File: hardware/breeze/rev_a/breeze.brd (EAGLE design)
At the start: 27.2 x 14.2 mm, 11 parts, among them J3 IMPULSE_GECKO_HEADER, U1 RV-3049-C3, U2 FM25V20-DG

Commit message: some parts on breeze
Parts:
- removed BT1: ML-1220/F1AN, batteries:ML-1220/F1BN
- removed C1: 10nF, passives:0402_CAP
- removed C2: 0.1uF, passives:0402_CAP
- removed R1, R2: 4.7k, passives:0402_RES
- removed R3, R4: 10k, passives:0402_RES
- removed U1: RV-3049-C3, chips:MICRO-CRYSTAL-C3
- removed U2: FM25V20-DG, chips:TDFN-8/6MM
- added Q1: NX3008PBK, fets:SOT23-3
- added R6: 100k, rcl:R0603
- moved LOGO1 5.76 mm to (2.69, 15.9)
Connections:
- removed net !FRAM_CS: J3.2, R1.1, U2.1
- removed net BATTERY: BT1.POS, C1.1, U1.2
- removed net N$6: R4.2, U1.9
- removed net N$7: R3.2, U1.1
- removed net RTC_CS: J3.4, R2.2, U1.8
- new net AIRFLOW_CTRL: J3.4, Q1.1, R6.1
- new net AIRFLOW_VCC: Q1.2
- new net TRIGGER: J3.2
- net GND: no longer BT1.NEG, C1.2, C2.2, R2.1, R3.1, R4.1, U1.6, U2.4
- net MISO0: no longer U1.5, U2.2
- net MOSI0: no longer U1.10, U2.5
- net SCLK0: no longer U1.4, U2.6
- net VCC: now also Q1.3, R6.2; no longer C2.1, R1.2, U2.3, U2.7, U2.8
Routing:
- net VCC: track 26.3 -> 0.00 mm, vias 3 -> 0
- net MISO0: track 23.9 -> 0.00 mm, vias 2 -> 0
- net !FRAM_CS: track 20.9 -> 0.00 mm, vias 2 -> 0
- net MOSI0: track 17.4 -> 0.00 mm, vias 2 -> 0
- net SCLK0: track 15.0 -> 0.00 mm
- net RTC_CS: track 6.19 -> 0.00 mm
- net BATTERY: track 5.69 -> 0.00 mm
- net GND: track 2.38 -> 0.00 mm, vias 20 -> 0
- net N$6: track 1.37 -> 0.00 mm
- net N$7: track 1.00 -> 0.00 mm
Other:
- board text removed: "+"
- board text removed: "-"

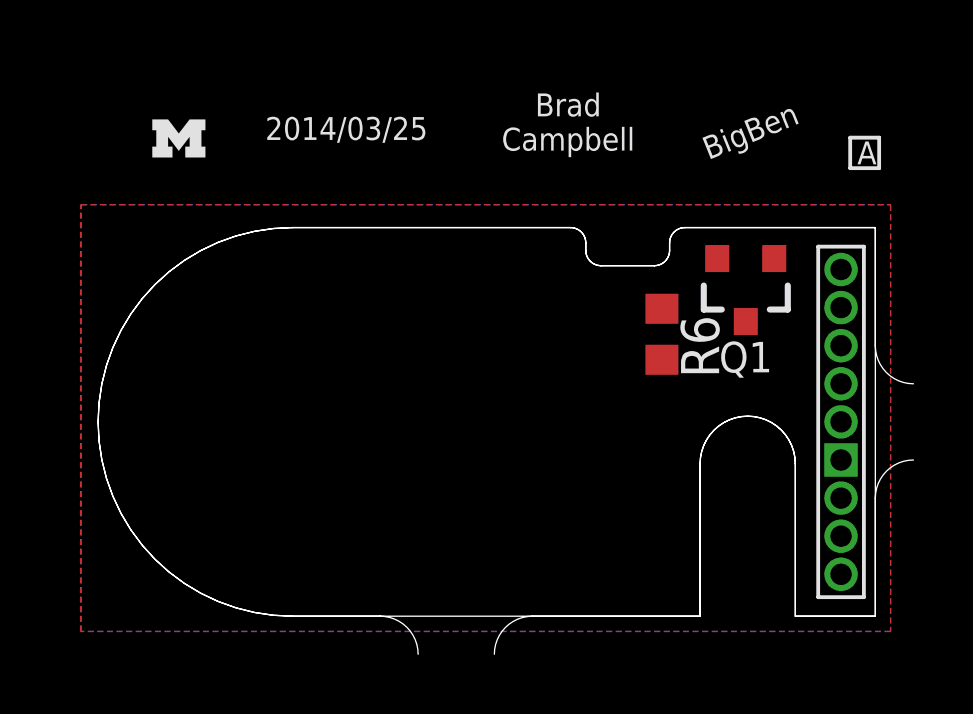
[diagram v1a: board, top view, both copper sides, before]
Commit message: simple breeze board routed
needs another pass when i get parts
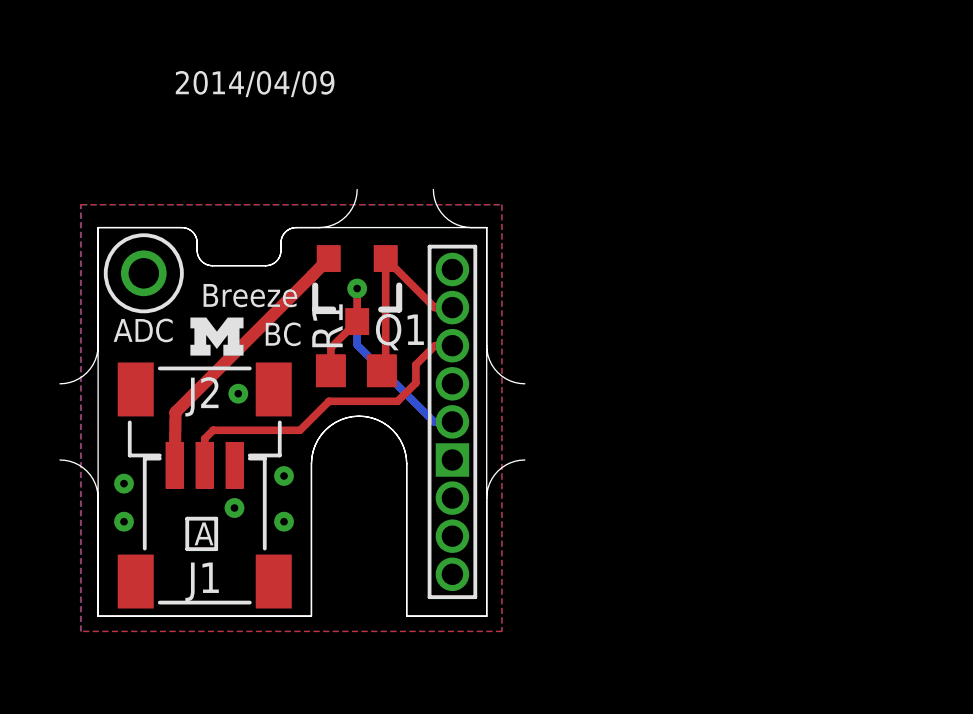
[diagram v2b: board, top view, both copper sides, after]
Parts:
- removed R6: 100k, rcl:R0603
- added J1: SH_MALE_1X3/1MM-RA, headers:1X3/SMD/SH/RA/1MM
- added J2: SH_MALE_1X3/1MM-TOP, headers:1X3/SMD/SH/1MM
- added R1: 100k, rcl:R0603
- added TP1: TEST_POINT_0.040IN, headers:TESTPOINT_0.040IN
- moved J3 13.0 mm to (11.8, 6.48)
- moved Q1 13.0 mm to (8.64, 10.9)
- moved LOGO1 6.73 mm to (3.96, 9.32)
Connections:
- removed net SHD: J3.3
- new net AIRFLOW_SIGNAL: J1.2, J2.2, J3.3, TP1.TESTPOINT
- net AIRFLOW_CTRL: now also R1.1; no longer R6.1
- net AIRFLOW_VCC: now also J1.1, J2.1
- net GND: now also J1.3, J2.3
- net VCC: now also R1.2; no longer R6.2
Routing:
- net AIRFLOW_SIGNAL: track 0.00 -> 10.8 mm
- net VCC: track 0.00 -> 9.22 mm, vias 0 -> 1
- net AIRFLOW_VCC: track 0.00 -> 9.00 mm
- net AIRFLOW_CTRL: track 0.00 -> 7.09 mm
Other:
- board size 27.2 x 14.2 mm -> 15.5 x 14.2 mm
- board text added: "2014/04/09"
- board text added: "ADC"
- board text added: "BC"
- board text added: "Breeze"
- board text removed: "2014/03/25"
- board text removed: "BigBen"
- board text removed: "Brad Campbell"

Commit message: connectted the analog pin to the testpoint
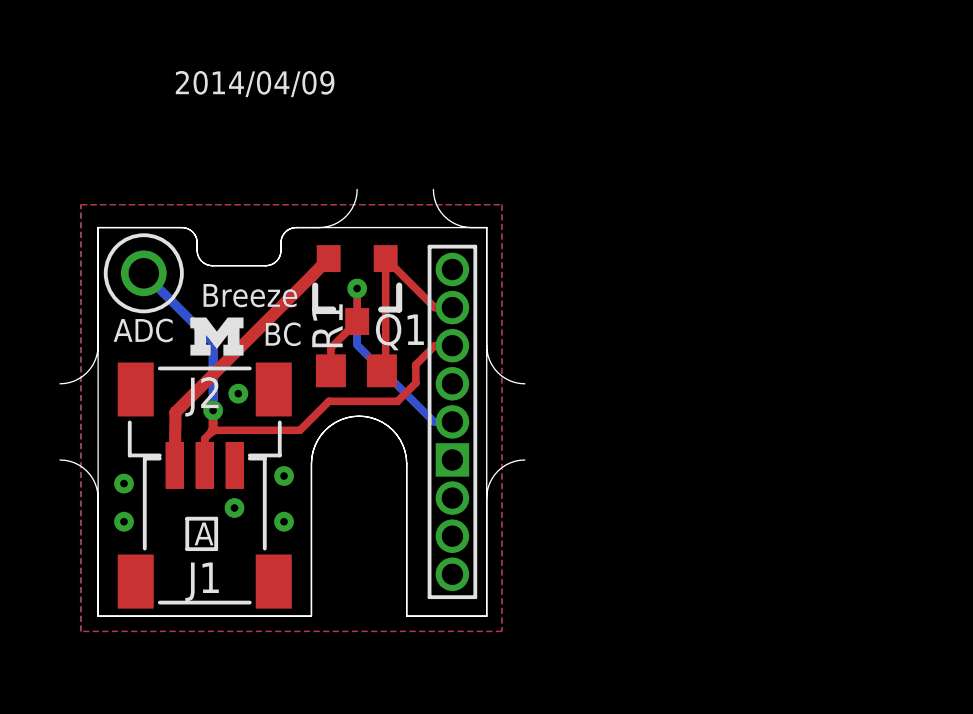
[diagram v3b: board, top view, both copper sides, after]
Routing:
- net AIRFLOW_SIGNAL: track 10.8 -> 17.0 mm, vias 0 -> 1
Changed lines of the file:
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@@
 <grid distance="0.01" unitdist="inch" unit="inch" style="lines" multiple="1" display="yes" altdistance="0.001" altunitdist="inch" altunit="inch"/>
 <layers>
-<layer number="1" name="Top" color="4" fill="1" visible="no" active="yes"/>
+<layer number="1" name="Top" color="4" fill="1" visible="yes" active="yes"/>
 <layer number="2" name="Route2" color="13" fill="10" visible="no" active="no"/>
 <layer number="3" name="Route3" color="4" fill="3" visible="no" active="no"/>
@@
 <layer number="14" name="Route14" color="1" fill="6" visible="no" active="no"/>
 <layer number="15" name="Route15" color="10" fill="2" visible="no" active="no"/>
-<layer number="16" name="Bottom" color="1" fill="1" visible="no" active="yes"/>
-<layer number="17" name="Pads" color="2" fill="1" visible="no" active="yes"/>
-<layer number="18" name="Vias" color="2" fill="1" visible="no" active="yes"/>
-<layer number="19" name="Unrouted" color="6" fill="1" visible="no" active="yes"/>
-<layer number="20" name="Dimension" color="15" fill="1" visible="no" active="yes"/>
-<layer number="21" name="tPlace" color="7" fill="1" visible="no" active="yes"/>
-<layer number="22" name="bPlace" color="7" fill="1" visible="no" active="yes"/>
-<layer number="23" name="tOrigins" color="15" fill="1" visible="no" active="yes"/>
-<layer number="24" name="bOrigins" color="15" fill="1" visible="no" active="yes"/>
-<layer number="25" name="tNames" color="7" fill="1" visible="no" active="yes"/>
+<layer number="16" name="Bottom" color="1" fill="1" visible="yes" active="yes"/>
+<layer number="17" name="Pads" color="2" fill="1" visible="yes" active="yes"/>
+<layer number="18" name="Vias" color="2" fill="1" visible="yes" active="yes"/>
+<layer number="19" name="Unrouted" color="6" fill="1" visible="yes" active="yes"/>
+<layer number="20" name="Dimension" color="15" fill="1" visible="yes" active="yes"/>
+<layer number="21" name="tPlace" color="7" fill="1" visible="yes" active="yes"/>
+<layer number="22" name="bPlace" color="7" fill="1" visible="yes" active="yes"/>
+<layer number="23" name="tOrigins" color="15" fill="1" visible="yes" active="yes"/>
+<layer number="24" name="bOrigins" color="15" fill="1" visible="yes" active="yes"/>
+<layer number="25" name="tNames" color="7" fill="1" visible="yes" active="yes"/>
 <layer number="26" name="bNames" color="7" fill="1" visible="no" active="yes"/>
 <layer number="27" name="tValues" color="7" fill="1" visible="no" active="yes"/>
@@
 <wire x1="2.5814" y1="6.7978" x2="7.1468" y2="11.3632" width="0.4064" layer="1"/>
 <wire x1="7.1468" y1="11.3632" x2="7.686" y2="11.922" width="0.4064" layer="1"/>
-<wire x1="2.556" y1="5.0332" x2="2.556" y2="5.029" width="0" layer="19" extent="1-1"/>
+<wire x1="2.556" y1="5.029" x2="2.556" y2="5.0332" width="0.3048" layer="1"/>
 </signal>
 <signal name="AIRFLOW_CTRL">
@@
 <wire x1="7.6962" y1="7.1628" x2="6.731" y2="6.1976" width="0.254" layer="1"/>
 <wire x1="6.731" y1="6.1976" x2="3.8354" y2="6.1976" width="0.254" layer="1"/>
-<wire x1="3.8354" y1="6.1976" x2="3.556" y2="5.9182" width="0.254" layer="1"/>
+<wire x1="3.7719" y1="6.1341" x2="3.556" y2="5.9182" width="0.254" layer="1"/>
 <wire x1="3.556" y1="5.9182" x2="3.556" y2="5.0332" width="0.254" layer="1"/>
 <wire x1="7.6962" y1="7.1628" x2="9.9822" y2="7.1628" width="0.254" layer="1"/>
 <wire x1="9.9822" y1="7.1628" x2="10.5918" y2="7.7724" width="0.254" layer="1"/>
 <wire x1="10.5918" y1="7.7724" x2="10.5918" y2="8.382" width="0.254" layer="1"/>
-<wire x1="3.8354" y1="6.1976" x2="1.524" y2="11.43" width="0" layer="19" extent="1-1"/>
-<wire x1="3.556" y1="5.029" x2="3.556" y2="5.0332" width="0" layer="19" extent="1-1"/>
+<wire x1="1.524" y1="11.43" x2="3.8354" y2="9.1186" width="0.3048" layer="16"/>
+<wire x1="3.8354" y1="9.1186" x2="3.8354" y2="6.858" width="0.3048" layer="16"/>
+<via x="3.8354" y="6.858" extent="1-16" drill="0.254"/>
+<wire x1="3.8354" y1="6.858" x2="3.8354" y2="6.1976" width="0.3048" layer="1"/>
+<wire x1="3.8354" y1="6.1976" x2="3.7719" y2="6.1341" width="0.3048" layer="1"/>
+<wire x1="3.556" y1="5.029" x2="3.556" y2="5.0332" width="0.3048" layer="1"/>
 </signal>
 </signals>

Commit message: updated breeze with low pass filter
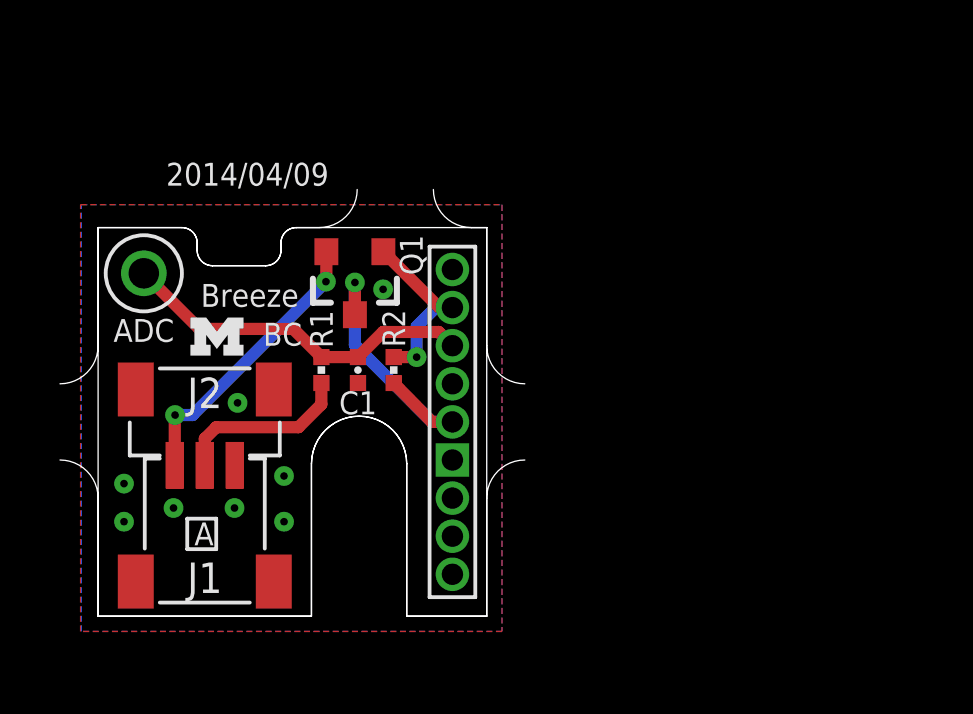
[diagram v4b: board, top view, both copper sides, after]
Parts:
- added C1: (no value), passives:0402_CAP
- added R2: 100k, passives:0402_RES
- R1: value 100k -> (none); device rcl:R0603 -> passives:0402_RES
- moved R1 1.17 mm to (7.44, 8.20), turned to 270 degrees
- moved Q1 0.24 mm to (8.56, 11.2)
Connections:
- new net AIRFLOW_SIGNAL_FILTERED: C1.1, J3.3, R1.1, TP1.TESTPOINT
- net AIRFLOW_CTRL: now also R2.1; no longer R1.1
- net AIRFLOW_SIGNAL: now also R1.2; no longer J3.3, TP1.TESTPOINT
- net GND: now also C1.2
- net VCC: now also R2.2; no longer R1.2
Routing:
- net AIRFLOW_SIGNAL_FILTERED: track 0.00 -> 12.0 mm
- net AIRFLOW_SIGNAL: track 17.0 -> 5.96 mm, vias 1 -> 0
- net AIRFLOW_CTRL: track 7.09 -> 6.31 mm, vias 0 -> 1
- net VCC: track 9.22 -> 9.97 mm
- net AIRFLOW_VCC: track 9.00 -> 9.56 mm, vias 0 -> 2
